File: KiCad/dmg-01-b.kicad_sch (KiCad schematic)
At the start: 59 parts, among them CN1 SCREEN, CN2 CART, CN3 EXT, CN4 BATTERY, P1 CART SHIELD GND PADS, P2 GND PAD, P3 GND PAD, P4 GND PAD, SW1 POWER_SW, U1 CPU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

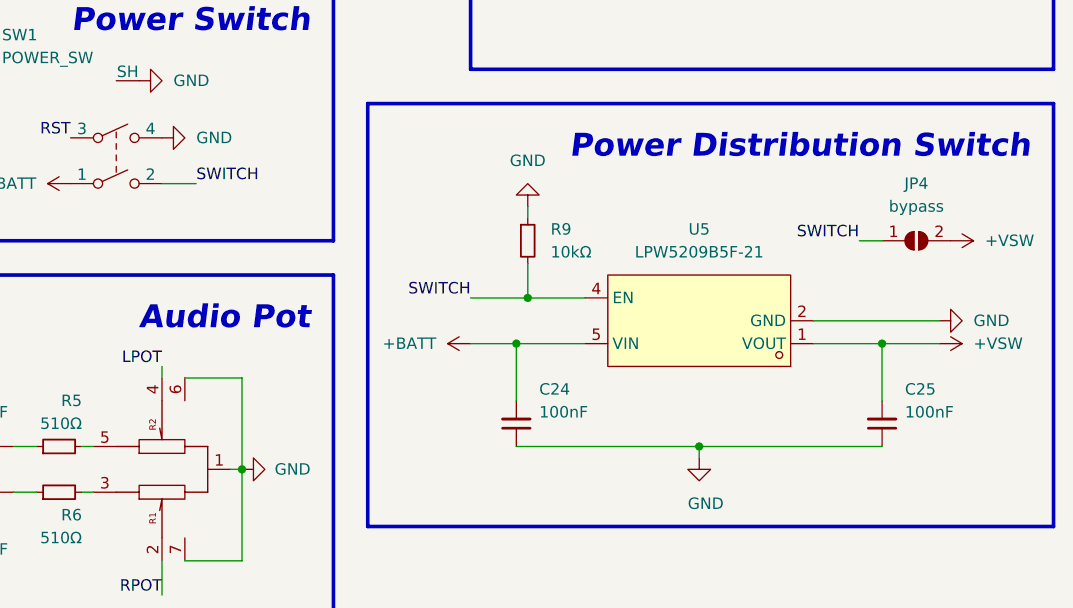
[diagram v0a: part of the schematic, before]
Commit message: minor tracks cleanup
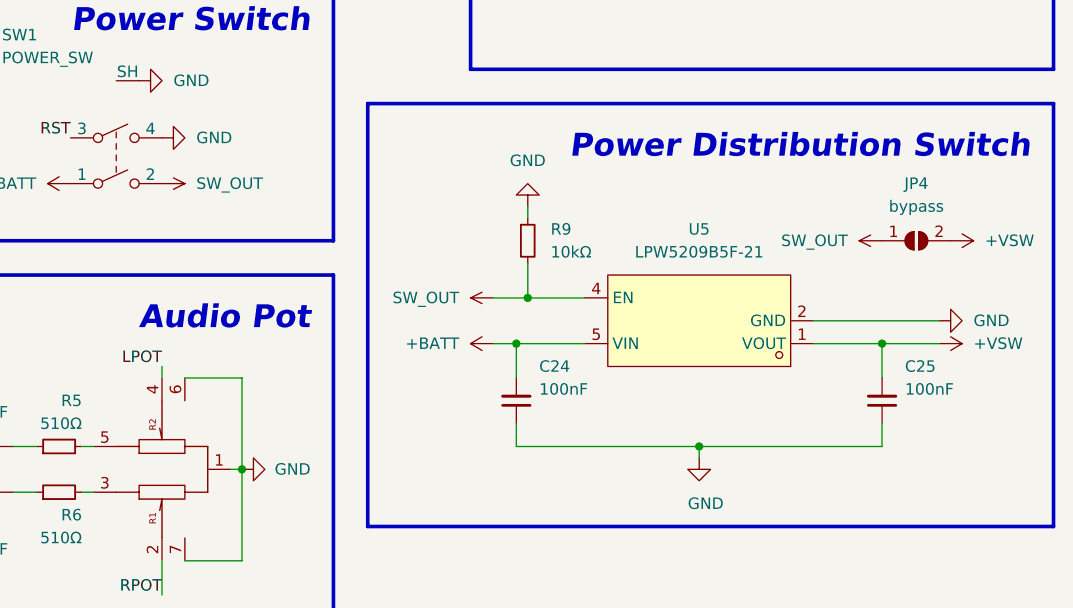
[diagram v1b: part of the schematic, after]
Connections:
- net SWITCH renamed SW_OUT
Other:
- moved on the sheet: C24, C25

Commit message: change side of 5v pin on the audio header
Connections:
- net +5V: now also H3.1 (VDD); no longer H3.5 (VDD)
- net AMP_EN: now also H3.5 (EN); no longer H3.4 (EN)
- net GND: now also H3.4 (GND); no longer H3.3 (GND)
- net LPOT: now also H3.2 (LEFT); no longer H3.1 (LEFT)
- net RPOT: now also H3.3 (RIGHT); no longer H3.2 (RIGHT)
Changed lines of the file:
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@@
     (stroke (width 0) (type default) (color 0 0 0 0))
   )
+  (wire (pts (xy 132.08 217.17) (xy 140.97 217.17))
+    (stroke (width 0) (type default) (color 0 0 0 0))
+  )
   (wire (pts (xy 124.46 180.34) (xy 132.08 180.34))
     (stroke (width 0) (type default) (color 0 0 0 0))
@@
     (stroke (width 0.4) (type default) (color 0 0 0 0))
   )
+  (wire (pts (xy 134.62 209.55) (xy 140.97 209.55))
+    (stroke (width 0) (type default) (color 0 0 0 0))
+  )
   (polyline (pts (xy 53.34 222.25) (xy 15.24 222.25))
     (stroke (width 0.4) (type default) (color 0 0 0 0))
@@
     (stroke (width 0) (type default) (color 0 0 0 0))
   )
-  (wire (pts (xy 132.08 212.09) (xy 140.97 212.09))
-    (stroke (width 0) (type default) (color 0 0 0 0))
-  )
   (text "USB\n" (at 158.75 86.36 180)
     (effects (font (size 2.54 2.54) (thickness 0.254) bold italic) (justify right bottom))
@@
     (effects (font (size 1.27 1.27)) (justify left bottom))
   )
-  (label "LPOT" (at 140.97 207.01 180)
+  (label "LPOT" (at 140.97 212.09 180)
     (effects (font (size 1.27 1.27)) (justify right bottom))
   )
@@
     (effects (font (size 1.27 1.27)) (justify left bottom))
   )
-  (label "RPOT" (at 140.97 209.55 180)
+  (label "RPOT" (at 140.97 214.63 180)
     (effects (font (size 1.27 1.27)) (justify right bottom))
   )
@@
     (effects (font (size 1.27 1.27)) (justify right bottom))
   )
-  (label "AMP_EN" (at 140.97 214.63 180)
+  (label "AMP_EN" (at 140.97 219.71 180)
     (effects (font (size 1.27 1.27)) (justify right bottom))
   )
@@
     (pin "9")
   )
-  (symbol (lib_id "power:+5V") (at 140.97 219.71 90) (unit 1)
+  (symbol (lib_id "power:+5V") (at 134.62 209.55 90) (unit 1)
     (in_bom yes) (on_board yes) (fields_autoplaced)
-    (property "Reference" "#PWR0124" (id 0) (at 144.78 219.71 0)
+    (property "Reference" "#PWR0124" (id 0) (at 138.43 209.55 0)
       (effects (font (size 1.27 1.27)) hide)
     )
-    (property "Value" "+5V" (id 1) (at 137.16 219.7099 90)
+    (property "Value" "+5V" (id 1) (at 130.81 209.5499 90)
       (effects (font (size 1.27 1.27)) (justify left))
     )
-    (property "Footprint" "" (id 2) (at 140.97 219.71 0)
+    (property "Footprint" "" (id 2) (at 134.62 209.55 0)
       (effects (font (size 1.27 1.27)) hide)
     )
-    (property "Datasheet" "" (id 3) (at 140.97 219.71 0)
+    (property "Datasheet" "" (id 3) (at 134.62 209.55 0)
       (effects (font (size 1.27 1.27)) hide)
     )
@@
     (pin "1")
   )
-  (symbol (lib_id "power:GND") (at 132.08 212.09 270) (unit 1)
+  (symbol (lib_id "power:GND") (at 132.08 217.17 270) (unit 1)
     (in_bom yes) (on_board yes)
-    (property "Reference" "#PWR0160" (id 0) (at 125.73 212.09 0)
+    (property "Reference" "#PWR0160" (id 0) (at 125.73 217.17 0)
       (effects (font (size 1.27 1.27)) hide)
     )
-    (property "Value" "GND" (id 1) (at 133.35 209.55 90)
+    (property "Value" "GND" (id 1) (at 133.35 214.63 90)
       (effects (font (size 1.27 1.27)) (justify right))
     )
-    (property "Footprint" "" (id 2) (at 132.08 212.09 0)
+    (property "Footprint" "" (id 2) (at 132.08 217.17 0)
       (effects (font (size 1.27 1.27)) hide)
     )
-    (property "Datasheet" "" (id 3) (at 132.08 212.09 0)
+    (property "Datasheet" "" (id 3) (at 132.08 217.17 0)
       (effects (font (size 1.27 1.27)) hide)
     )
@@
     (pin "1")
   )
-  (symbol (lib_id "kmc_lib:DMGB_AUDIO_HEADER") (at 137.16 203.2 0) (unit 1)
+  (symbol (lib_id "kmc_lib:DMGB_AUDIO_HEADER") (at 137.16 205.74 0) (unit 1)
     (in_bom no) (on_board yes)
     (property "Reference" "H3" (id 0) (at 139.7 223.52 0)
@@
       (effects (font (size 1.27 1.27)) (justify left))
     )
-    (property "Footprint" "kmc_lib:2.54_PAD_SMD_X5" (id 2) (at 137.16 203.2 0)
+    (property "Footprint" "kmc_lib:2.54_PAD_SMD_X5" (id 2) (at 137.16 205.74 0)
       (effects (font (size 1.27 1.27)) hide)
     )
-    (property "Datasheet" "" (id 3) (at 137.16 203.2 0)
+    (property "Datasheet" "" (id 3) (at 137.16 205.74 0)
       (effects (font (size 1.27 1.27)) hide)
     )

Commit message: more pedantic changes
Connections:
- net +VSW renamed PD_OUT
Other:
- moved on the sheet: C25, JP4

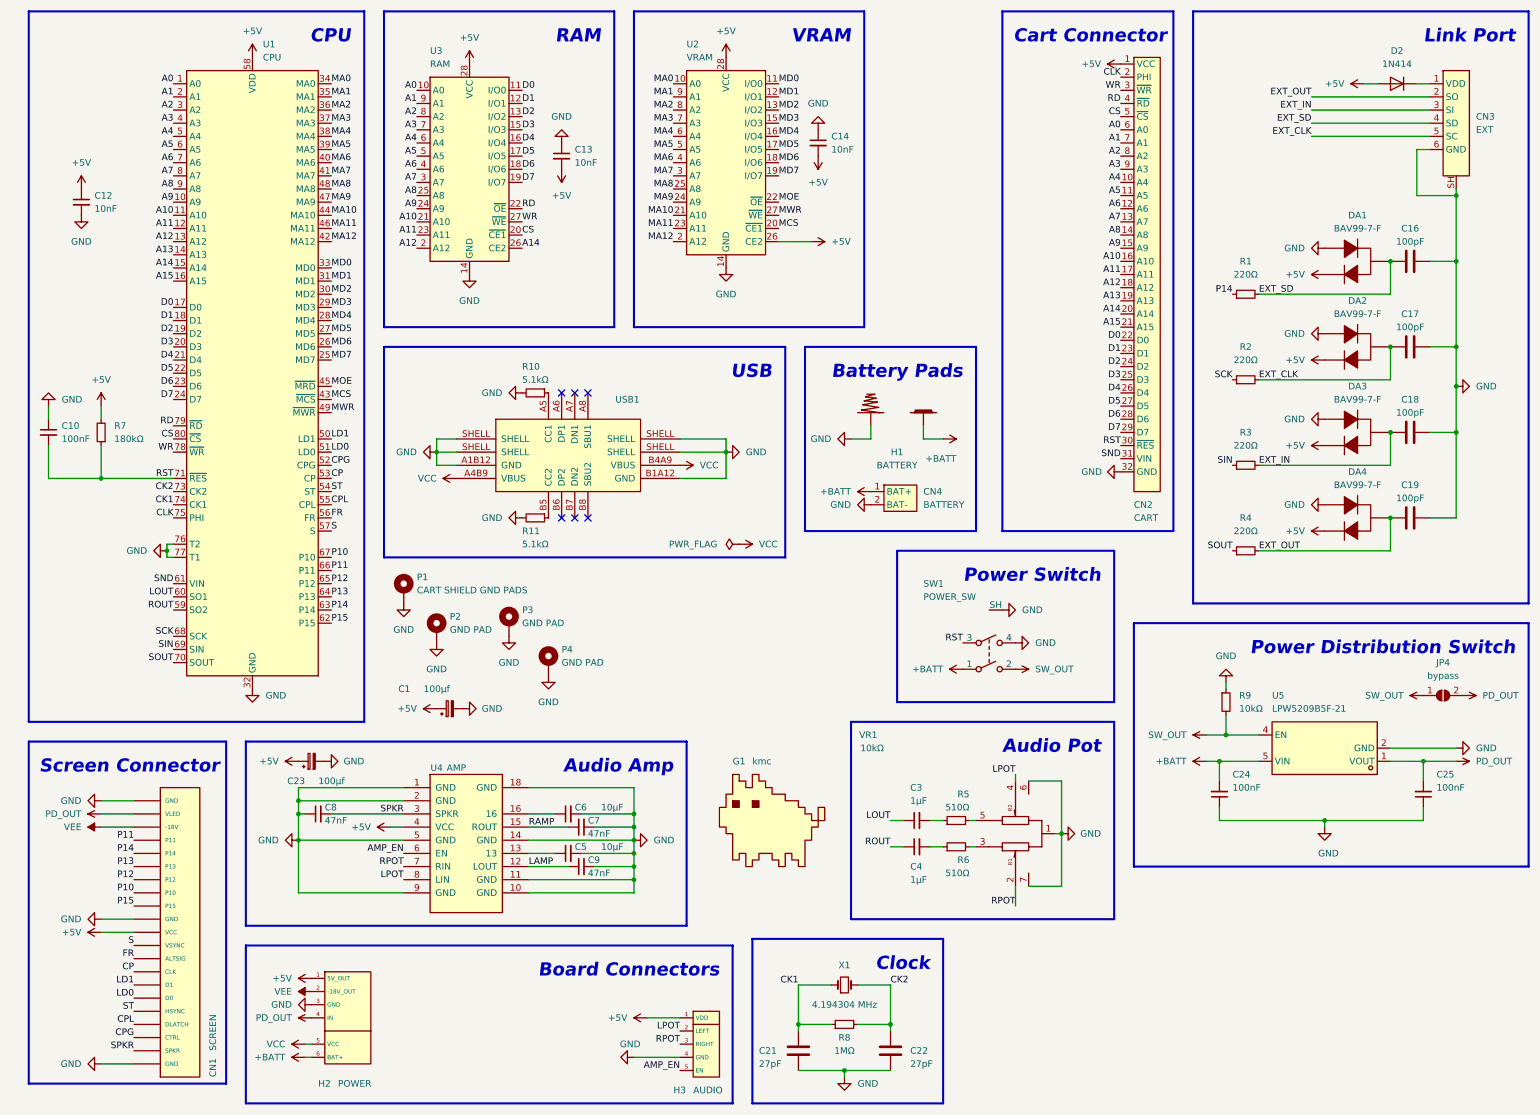
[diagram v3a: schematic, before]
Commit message: better bottom pads
- more clearance between the battery terminals and bottom pads
- swapped +bat and usb on the power pads because it makes more sense
- marked more clearly where the og boards go
- small routing optimizations
- small cosmetic changes
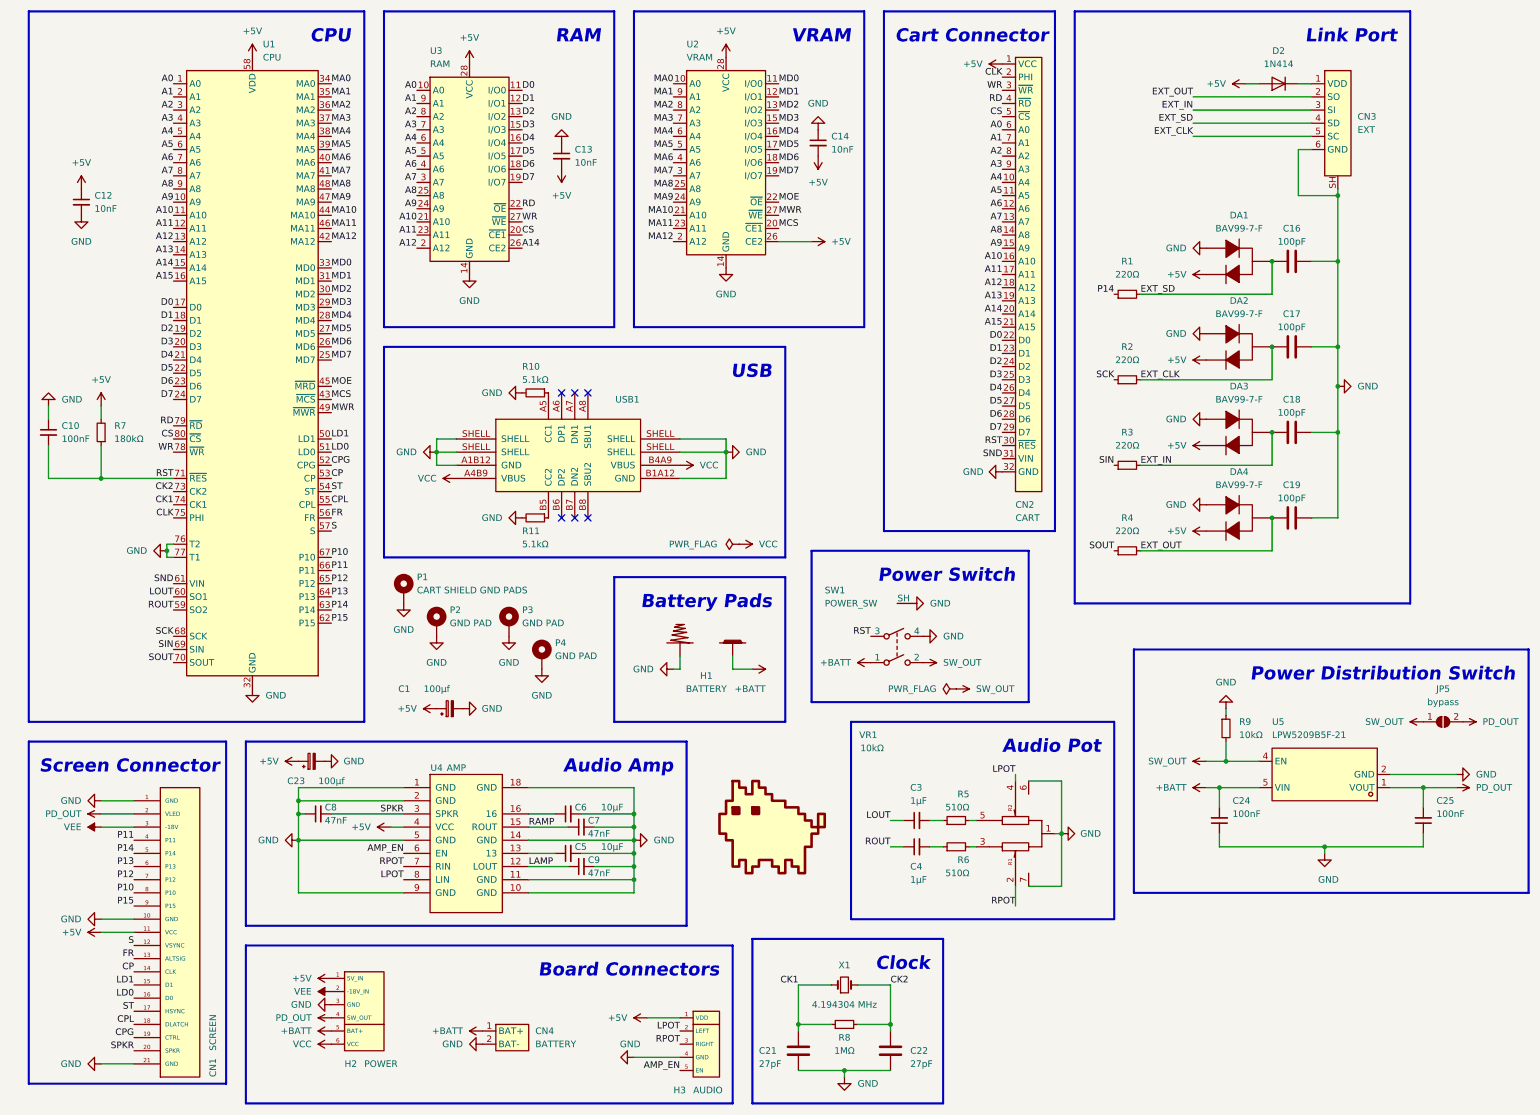
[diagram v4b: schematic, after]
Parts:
- removed JP4: bypass, kmc_lib:solder_jumper_x2, symbol Jumper:SolderJumper_2_Open
- added JP5: bypass, kmc_lib:solder_jumper_x2, symbol Jumper:SolderJumper_2_Open
- CN1: footprint dmg_lib:DMG_FPC_CONN -> kmc_lib:DMG_FPC_CONN
- H2: footprint kmc_lib:2.54_PAD_SMD_X6 -> kmc_lib:PAD_2.54_HYBRID_X6
- H3: footprint kmc_lib:2.54_PAD_SMD_X5 -> kmc_lib:PAD_2.54_HYBRID_X5
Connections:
- net +BATT: now also H2.5 (BAT+); no longer H2.6 (BAT+)
- net PD_OUT: now also JP5.2 (B)
- net SW_OUT: now also JP5.1 (A)
- net VCC: now also H2.6 (VCC); no longer H2.5 (VCC)
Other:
- moved on the sheet: C16, C17, C18, C19, CN2, CN3, CN4, D2, DA1, DA2, DA3, DA4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
